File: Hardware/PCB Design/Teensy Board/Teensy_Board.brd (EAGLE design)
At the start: 98.7 x 81.3 mm, 44 parts, among them IC1 MC7805BDTRKG, IC2 UA78M33CKVU, Q1 PROGRAM_FET, U1 PCA9685PW, U2 74HC4051PW,118, U3 74HC4051PW,118, X1 RJ45-8X, X2 RJ45-8X, X3 RJ45-8X, X4 RJ45-8X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

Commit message: Added BOM for latest PCB version
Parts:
- R7, R8: value (none) -> 2.2k
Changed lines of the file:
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@@
 </element>
 <element name="X8" library="CBLA_Test_bed_Library" package="1X02" value="UART" x="37.338" y="76.2" rot="R90"/>
-<element name="R7" library="CBLA_Test_bed_Library" package="R0603" value="" x="39.37" y="33.782" rot="R270"/>
-<element name="R8" library="CBLA_Test_bed_Library" package="R0603" value="" x="58.928" y="43.18" rot="R270"/>
+<element name="R7" library="CBLA_Test_bed_Library" package="R0603" value="2.2k" x="39.37" y="33.782" rot="R270"/>
+<element name="R8" library="CBLA_Test_bed_Library" package="R0603" value="2.2k" x="58.928" y="43.18" rot="R270"/>
 <element name="X7" library="con-wago-508" package="W237-4P" value="" x="74.676" y="5.334">
 <attribute name="OC_NEWARK" value="unknown" x="74.676" y="5.334" size="1.778" layer="27" display="off"/>

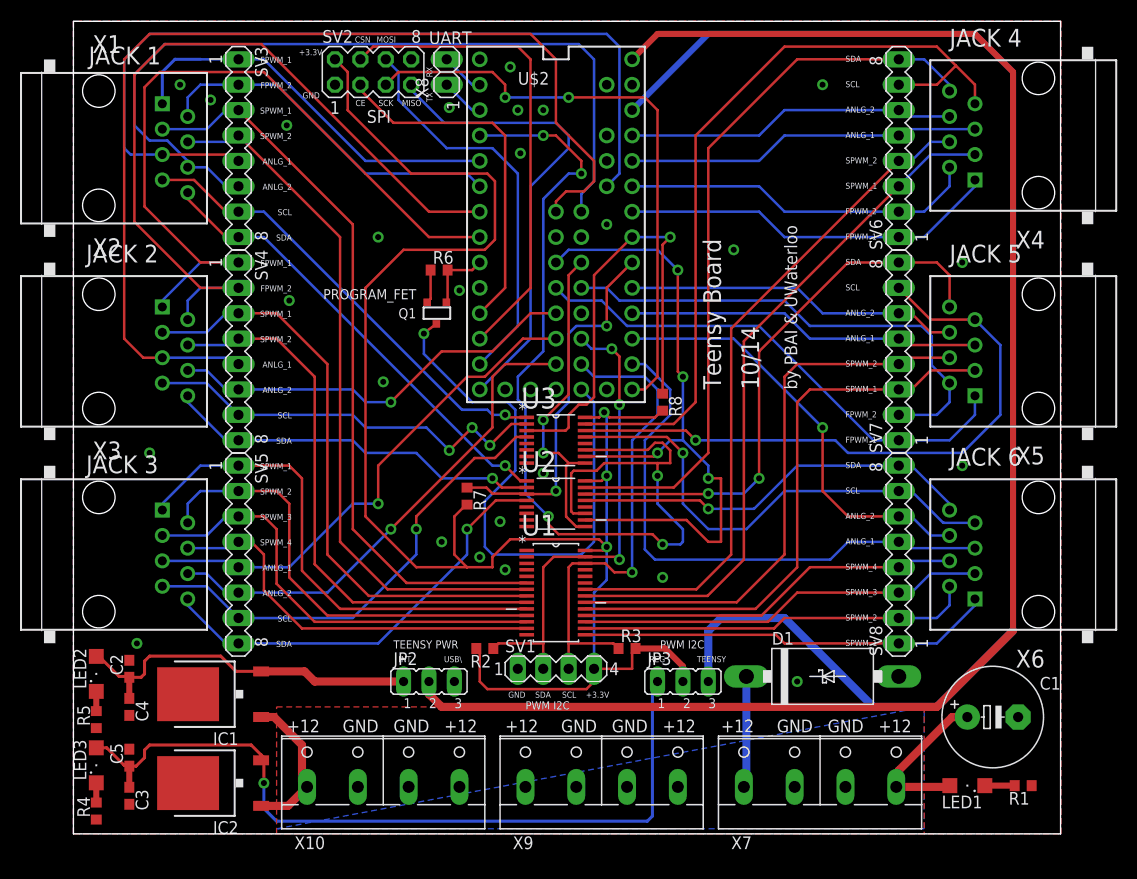
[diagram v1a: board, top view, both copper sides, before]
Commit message: Fixed the power plate error and misplacement of port #4
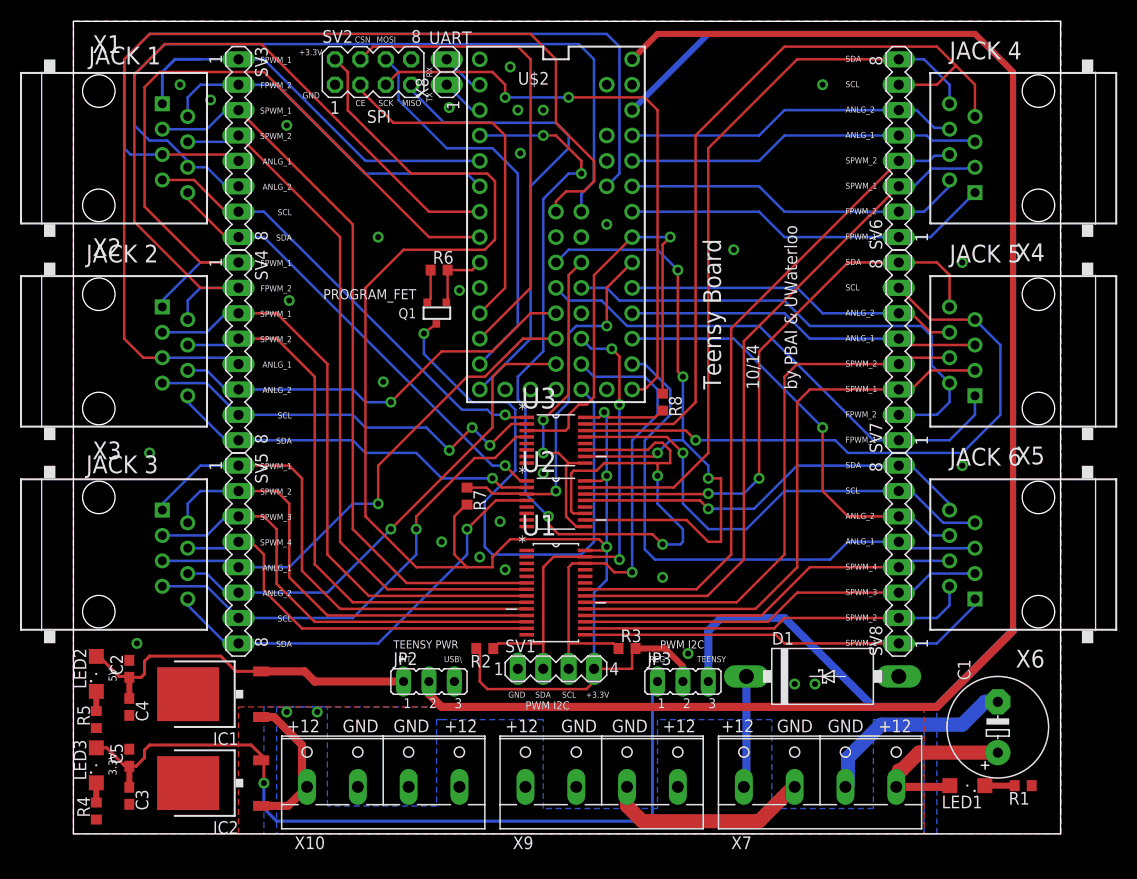
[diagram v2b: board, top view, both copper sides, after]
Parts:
- moved X4 1.27 mm to (96.5, 68.6)
- moved C1 1.14 mm to (92.5, 10.7), turned to 90 degrees
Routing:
- net GND: track 3.36 -> 44.5 mm, vias 26 -> 28
- net +12V: track 42.4 -> 44.0 mm, vias 0 -> 2
- net MUL_SCL_4: track 80.2 -> 81.5 mm
- net MUL_SDA_4: track 73.7 -> 75.0 mm
- net FPWM_4_2: track 35.8 -> 34.5 mm
- net FPWM_4_1: track 38.1 -> 37.2 mm
- net SPWM_4_2: track 68.2 -> 67.7 mm
- net SPWM_4_1: track 70.1 -> 69.5 mm
- net A9: track 33.1 -> 33.6 mm
- added copper zone on layer 16, net +12V
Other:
- board text added: "3.3V"
- board text added: "5V"

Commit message: Made Teensy Board smaller by moving the RJ45 connector to another board
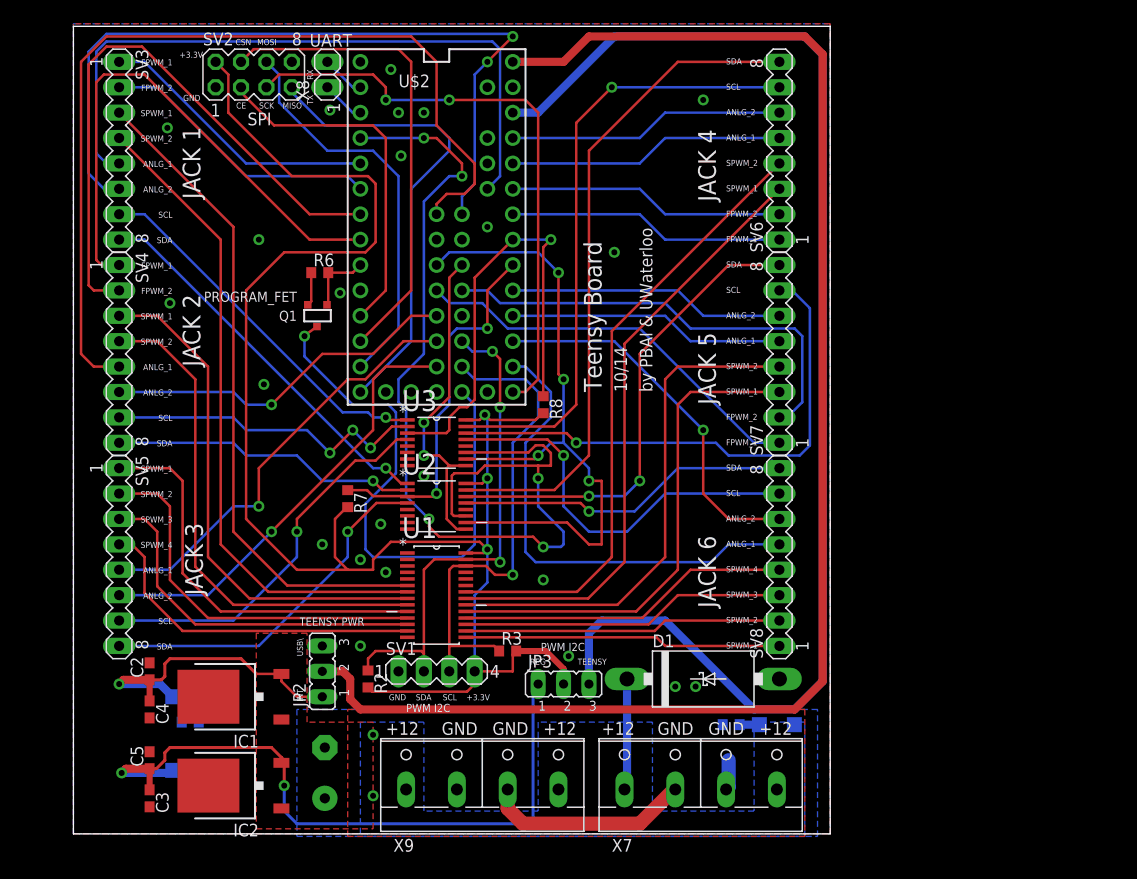
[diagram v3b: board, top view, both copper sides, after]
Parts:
- removed X1, X2, X3, X4, X5, X6: RJ45-8X, CBLA_Test_bed_Library:RJ45-NO-SHIELD
- removed X10: (no value), con-wago-508:W237-4P
- moved C1 67.5 mm to (25.1, 6.10), flipped to the bottom
- moved R1 29.8 mm to (65.8, 10.9), flipped to the bottom
- moved LED1 20.0 mm to (70.4, 10.9), flipped to the bottom
- moved R2 12.1 mm to (29.5, 15.5), turned to 270 degrees
- moved D1 11.9 mm to (63.0, 15.5)
- moved JP3 11.9 mm to (49.0, 15.0)
- moved Q1 11.9 mm to (24.4, 51.8)
- moved R3 11.9 mm to (43.4, 18.3)
- moved SV2 11.9 mm to (18.0, 75.9)
- moved SV3 11.9 mm to (4.57, 68.3)
- moved SV4 11.9 mm to (4.57, 48.0)
- moved SV5 11.9 mm to (4.57, 27.7)
- moved SV6 11.9 mm to (70.6, 68.3)
- moved SV7 11.9 mm to (70.6, 48.0)
- moved SV8 11.9 mm to (70.6, 27.7)
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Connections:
- net +12V: no longer X10.1, X10.4
- net A0: no longer X6.5
- net A1: no longer X6.6
- net A11: no longer X1.5
- net A12: no longer X2.5
- net A13: no longer X1.6
- net A15: no longer X2.6
- net A16: no longer X3.5
- net A17: no longer X3.6
- net A2: no longer X5.5
- net A3: no longer X5.6
- net A8: no longer X4.5
- net A9: no longer X4.6
- net FPWM_1_1: no longer X1.1
- net FPWM_1_2: no longer X1.2
- net FPWM_2_1: no longer X2.1
- net FPWM_2_2: no longer X2.2
- net FPWM_4_1: no longer X4.1
- net FPWM_4_2: no longer X4.2
- net FPWM_5_1: no longer X5.1
- net FPWM_5_2: no longer X5.2
- net GND: no longer X10.2, X10.3
- net MUL_SCL_1: no longer X1.7
- net MUL_SCL_2: no longer X2.7
- net MUL_SCL_3: no longer X3.7
- net MUL_SCL_4: no longer X4.7
- net MUL_SCL_5: no longer X5.7
- net MUL_SCL_6: no longer X6.7
- net MUL_SDA_1: no longer X1.8
- net MUL_SDA_2: no longer X2.8
- net MUL_SDA_3: no longer X3.8
- net MUL_SDA_4: no longer X4.8
- net MUL_SDA_5: no longer X5.8
- net MUL_SDA_6: no longer X6.8
- net SPWM_1_1: no longer X1.3
- net SPWM_1_2: no longer X1.4
- net SPWM_2_1: no longer X2.3
- net SPWM_2_2: no longer X2.4
- net SPWM_3_1: no longer X3.1
- net SPWM_3_2: no longer X3.2
- net SPWM_3_3: no longer X3.3
- net SPWM_3_4: no longer X3.4
- net SPWM_4_1: no longer X4.3
- net SPWM_4_2: no longer X4.4
- net SPWM_5_1: no longer X5.3
- net SPWM_5_2: no longer X5.4
- net SPWM_6_1: no longer X6.1
- net SPWM_6_2: no longer X6.2
- net SPWM_6_3: no longer X6.3
- net SPWM_6_4: no longer X6.4
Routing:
- net +12V: track 44.0 -> 11.2 mm
- net FPWM_2_1: track 75.2 -> 53.8 mm
- net MUL_SCL_4: track 81.5 -> 61.9 mm, vias 0 -> 1
- net A11: track 86.5 -> 68.5 mm
- net FPWM_2_2: track 79.4 -> 61.5 mm
- net GND: track 44.5 -> 27.2 mm, vias 28 -> 23
- net A12: track 105.1 -> 90.6 mm
- net FPWM_1_1: track 40.3 -> 28.3 mm
- net FPWM_5_1: track 51.2 -> 40.6 mm
- net TEENSY_VIN: track 160.0 -> 149.5 mm
- net MUL_SCL_5: track 63.5 -> 53.3 mm
- net TEENSY_3V3: track 141.6 -> 131.4 mm
- net +3V3: track 80.4 -> 70.5 mm, vias 1 -> 2
- net SPWM_6_1: track 41.6 -> 31.7 mm
- net SPWM_3_1: track 50.0 -> 40.2 mm
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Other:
- board size 98.7 x 81.3 mm -> 75.7 x 80.8 mm
